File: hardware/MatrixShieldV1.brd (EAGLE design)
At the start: 48.5 x 36.8 mm, 11 parts, among them J1 CON_HEADER_2X08-PTH-SHROUDED, J4 1X2-5.0

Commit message: Cleaned up schematic Added license to schematic and board
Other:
- board text added: "Pixelmatix 2014 CC BY-SA"
- board text added: "Rev V1"
- board text added: "SmartMatrix Shield for Teensy 3"
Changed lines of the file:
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@@
 <layer number="20" name="Dimension" color="15" fill="1" visible="yes" active="yes"/>
 <layer number="21" name="tPlace" color="7" fill="1" visible="yes" active="yes"/>
-<layer number="22" name="bPlace" color="7" fill="1" visible="yes" active="yes"/>
+<layer number="22" name="bPlace" color="7" fill="1" visible="no" active="yes"/>
 <layer number="23" name="tOrigins" color="15" fill="1" visible="yes" active="yes"/>
 <layer number="24" name="bOrigins" color="15" fill="1" visible="yes" active="yes"/>
@@
 <layer number="46" name="Milling" color="3" fill="1" visible="no" active="yes"/>
 <layer number="47" name="Measures" color="7" fill="1" visible="no" active="yes"/>
-<layer number="48" name="Document" color="7" fill="1" visible="no" active="yes"/>
+<layer number="48" name="Document" color="7" fill="1" visible="yes" active="yes"/>
 <layer number="49" name="Reference" color="7" fill="1" visible="no" active="yes"/>
 <layer number="50" name="dxf" color="7" fill="1" visible="no" active="no"/>
-<layer number="51" name="tDocu" color="7" fill="1" visible="no" active="yes"/>
+<layer number="51" name="tDocu" color="7" fill="1" visible="yes" active="yes"/>
 <layer number="52" name="bDocu" color="7" fill="1" visible="yes" active="yes"/>
 <layer number="53" name="tGND_GNDA" color="7" fill="9" visible="no" active="no"/>
@@
 <text x="14.478" y="29.21" size="1.27" layer="22" font="vector" ratio="12" rot="SMR0">GND</text>
 <text x="21.59" y="29.21" size="1.27" layer="22" font="vector" ratio="12" rot="MR0">5V</text>
+<text x="-0.254" y="-6.604" size="1.778" layer="48">Pixelmatix 2014 CC BY-SA</text>
+<text x="0" y="-3.556" size="1.778" layer="48">SmartMatrix Shield for Teensy 3</text>
+<text x="48.768" y="-3.302" size="1.778" layer="48" align="bottom-right">Rev V1</text>
 </plain>
 <attributes>

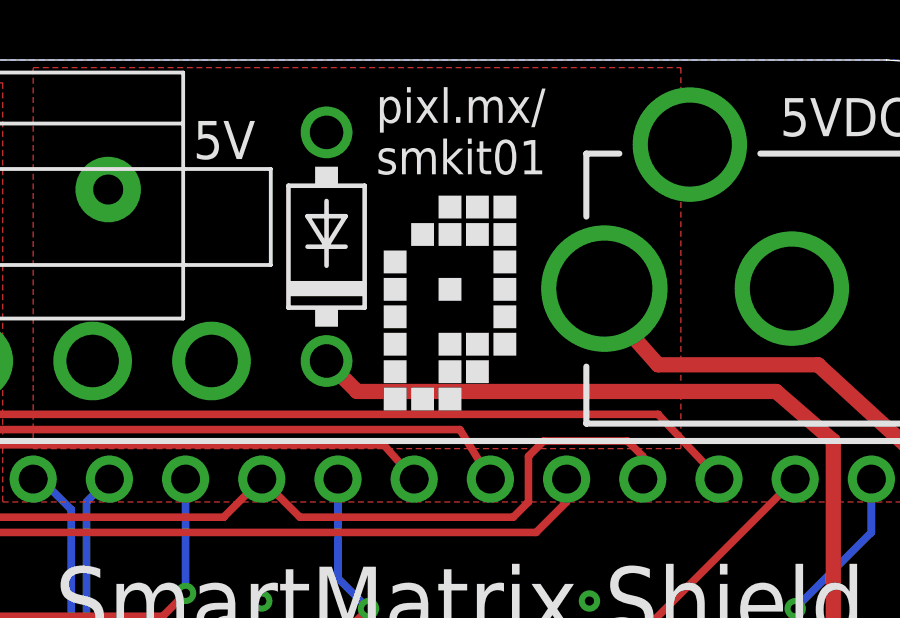
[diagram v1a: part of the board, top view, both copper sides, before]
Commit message: removed pixelmatix logo from board
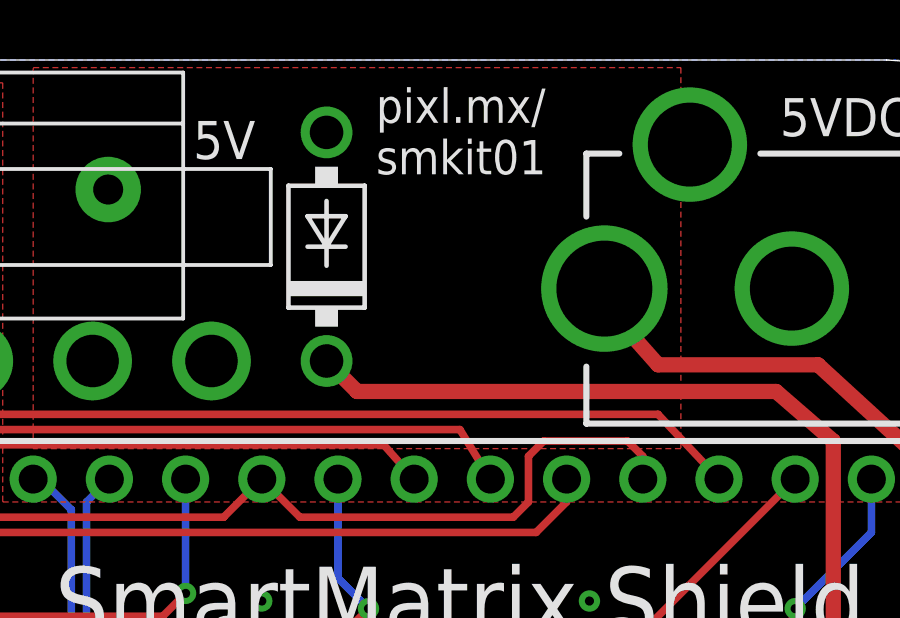
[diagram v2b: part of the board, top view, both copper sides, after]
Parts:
- removed U$4: (no value), eclibrary:PIXELMATIX-LOGO-300
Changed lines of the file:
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@@
 </element>
 <element name="J4" library="eclibrary" package="1X2-5.0MM" value="1X2-5.0" x="16.51" y="32.512" smashed="yes" rot="R180"/>
-<element name="U$4" library="eclibrary" package="PIXELMATIX-LOGO-300" value="" x="28.194" y="25.146"/>
 </elements>
 <signals>
